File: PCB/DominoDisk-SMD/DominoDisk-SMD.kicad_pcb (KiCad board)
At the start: 2 copper layers, 45.7 x 38.9 mm, 33 parts, among them J1 Daisy port out, J2 ICSP_ISP6, J3 UART, J4 Daisy port in, K1 HYC77-TF09-200, U1 PC817C-S, U2 ATmega328P-AU, U3 SE5218, U4 TXB0104PWR, Y1 Resonator

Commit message: More OCD
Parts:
- J4: renamed from J3; moved to B.Cu
- moved R5 14.2 mm to (137.1, 51.9), turned to -90 degrees
- moved C7 3.84 mm to (117.9, 60.5), turned to 0 degrees
- moved J4 2.74 mm to (104.0, 67.4)
- moved R7 2.15 mm to (117.7, 52.3)
- moved C5 1.97 mm to (119.2, 52.3), turned to 90 degrees
- moved C6 1.92 mm to (122.5, 60.5)
- moved G*** 1.54 mm to (136.6, 60.0), turned to 90 degrees
- moved U4 1.53 mm to (120.2, 56.9)
- moved C4 1.52 mm to (125.0, 52.3)
- moved Y1 1.48 mm to (104.5, 62.5)
- moved U2 1.39 mm to (122.1, 52.3)
- moved C8 0.93 mm to (108.0, 62.7)
- moved R2 0.89 mm to (128.5, 53.2), turned to 0 degrees
- moved U3 0.78 mm to (107.0, 56.0)
- moved U1 0.25 mm to (132.3, 50.1)
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- renumbered C5 to C1, C6 to C2, C7 to C3, C8 to C4, C4 to C5, C9 to C6, C10 to C7, C2 to C8, D3 to D1, D1 to D2, D2 to D3, J4 to J3, R6 to R1, R4 to R2, R1 to R3, R3 to R4, R2 to R6, REF** to REF**1, REF** to REF**2, REF** to REF**3, REF** to REF**4, U3 to U2, U2 to U3
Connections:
- K1 pad SHIELD: (no net) -> GND
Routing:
- net HDSEL_in: track 8.24 -> 25.9 mm
- net 5V_burgerDisk: track 68.6 -> 56.3 mm, vias 5 -> 4
- net GND: track 124.4 -> 135.1 mm, vias 13 -> 11
- net WRPROT_out: track 40.6 -> 30.7 mm, vias 1 -> 2
- net DRV1_in: track 40.6 -> 45.6 mm
- net OE: track 4.05 -> 7.53 mm
- net TX: track 13.0 -> 16.3 mm
- net RESET: track 34.9 -> 37.8 mm
- net DRV2_out: track 35.3 -> 38.1 mm
- net WRPROT_in: track 44.1 -> 46.8 mm
- net Net-(U3-XTAL2/PB7): track 3.35 -> 1.20 mm
- net DRV2_burgerDisk: track 35.6 -> 37.6 mm
- net PH1: track 28.7 -> 27.3 mm
- net 3V3: track 21.2 -> 19.8 mm, vias 1 -> 2
- net PH0: track 25.8 -> 24.5 mm
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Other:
- board text added: "© Colin Leroy-Mira https://colino.net"

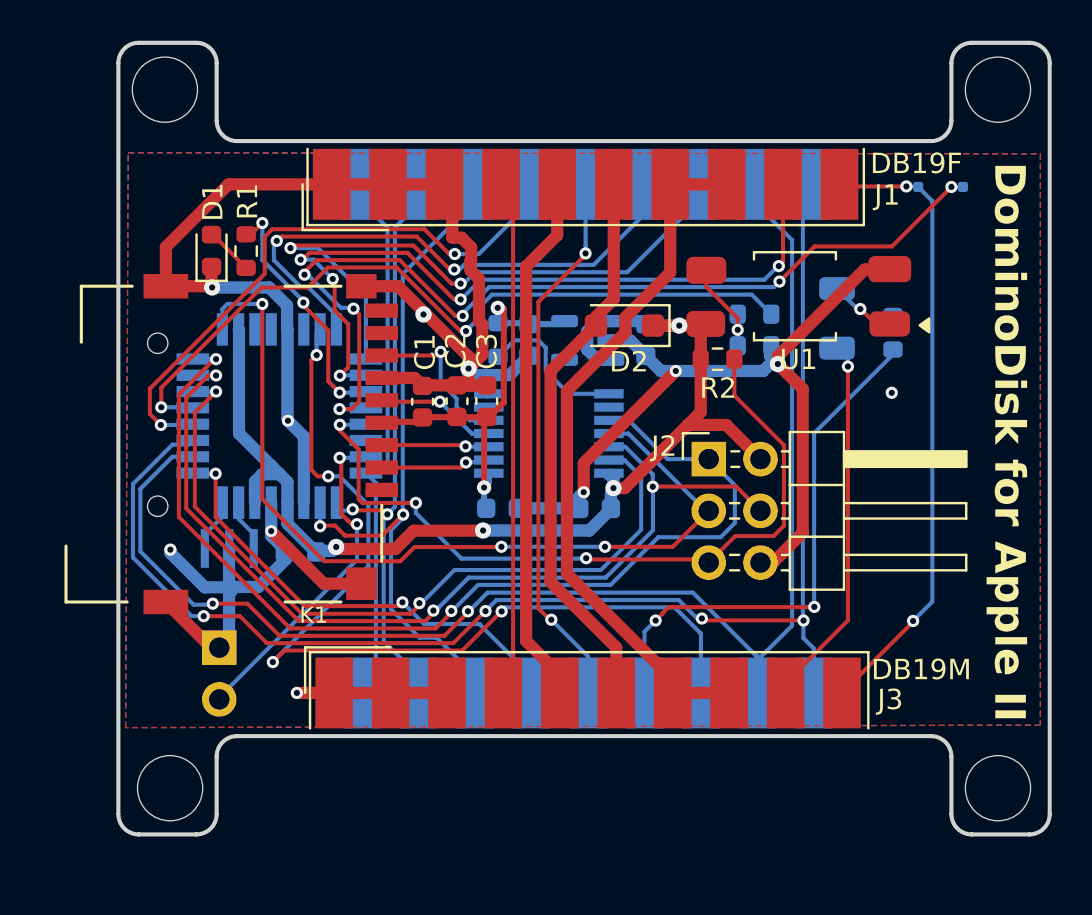
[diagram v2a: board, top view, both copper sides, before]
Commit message: Enable teardrops
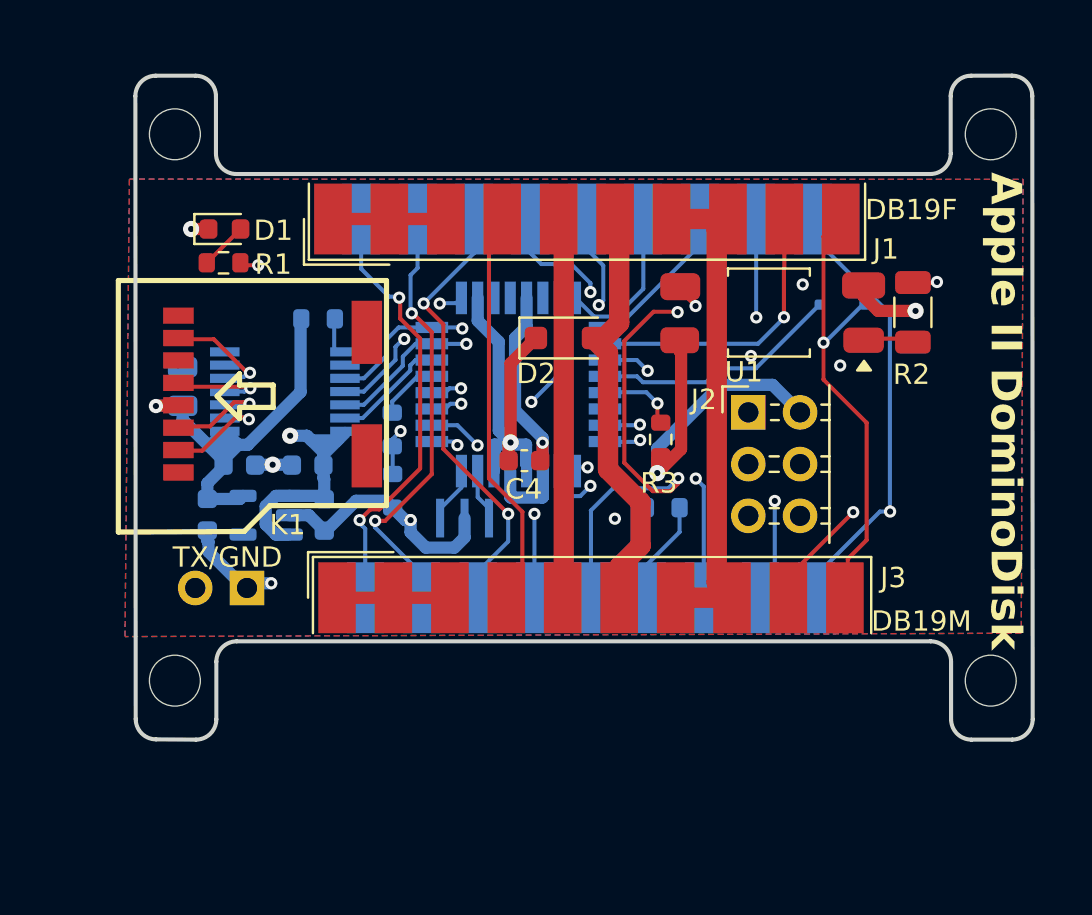
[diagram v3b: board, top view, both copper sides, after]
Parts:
- removed the C1 at (114.0, 55.3)
- removed the C2 at (115.7, 55.3)
- C1: renamed from C3; value 100n -> 22uF; footprint Capacitor_SMD:C_0603_1608Metric -> Capacitor_SMD:C_0805_2012Metric; moved to B.Cu
- C4: renamed from C8; moved to F.Cu
- J4: footprint Connector_PinHeader_2.54mm:PinHeader_1x02_P2.54mm_Horizontal -> Connector_PinHeader_2.54mm:PinHeader_1x02_P2.54mm_Vertical
- K1: value HYC77-TF09-200 -> TF-104; footprint HYC04-TF09-200:MICROSD-HYC77-TF09-200 -> TF-104:TF-SMD_TF-104
- R2: renamed from R3; moved to F.Cu
- REF**1, REF**2, REF**3, REF**4: value MountingHole_3.2mm_M3 -> MountingHole_2.5mm; footprint MountingHole:MountingHole_3.2mm_M3 -> MountingHole:MountingHole_2.5mm
- moved R6 19.1 mm to (112.5, 59.7), turned to 90 degrees
- moved R5 18.7 mm to (112.5, 56.7), turned to -90 degrees
- moved C5 18.0 mm to (109.2, 60.9)
- moved C6 18.0 mm to (103.5, 60.8)
- moved U4 18.0 mm to (106.3, 60.9)
- moved C1 14.9 mm to (102.2, 54.5)
- moved C2 14.3 mm to (108.4, 58.4)
- moved R7 14.2 mm to (125.8, 60.5), turned to 0 degrees
- moved U3 13.1 mm to (107.3, 54.8)
- moved C3 13.1 mm to (105.0, 58.4)
- moved C4 11.9 mm to (119.0, 58.2), turned to 0 degrees
- moved U2 11.8 mm to (118.7, 54.5)
- moved Y1 11.6 mm to (116.1, 61.0)
- moved R4 8.89 mm to (108.9, 51.2), turned to 0 degrees
- moved D3 7.53 mm to (134.6, 50.5), turned to 0 degrees
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- renumbered C6 to C2, C7 to C3, C4 to C5, C5 to C6, R2 to R3, R7 to R4, R4 to R5, R5 to R7, U3 to U2, U4 to U3, U2 to U4
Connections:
- K1 pad 9: (no net) -> GND
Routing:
- net GND: track 135.4 -> 48.7 mm, vias 11 -> 10
- net DRV2_burgerDisk: track 37.6 -> 3.00 mm, vias 2 -> 0
- net WRPROT_in: track 46.6 -> 12.2 mm, vias 6 -> 0
- net CS: track 37.6 -> 5.59 mm, vias 2 -> 0
- net MISO: track 50.8 -> 23.0 mm, vias 2 -> 1
- net RESET: track 37.8 -> 10.9 mm, vias 3 -> 1
- net RDDATA: track 66.3 -> 39.7 mm, vias 2 -> 3
- net DRV1_in: track 45.6 -> 21.8 mm, vias 4 -> 2
- net DRV2_out: track 37.7 -> 14.2 mm, vias 5 -> 1
- net DRV1_out: track 30.3 -> 6.93 mm, vias 2 -> 0
- net MOSI: track 46.9 -> 26.1 mm, vias 3 -> 1
- net HDSEL_in: track 25.9 -> 5.07 mm, vias 2 -> 0
- net WRDATA: track 68.2 -> 49.5 mm, vias 4 -> 2
- net Net-(R5-Pad2): track 5.36 -> 23.7 mm, vias 1 -> 2
- net HDSEL_out: track 25.0 -> 6.67 mm, vias 2 -> 0
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- added copper zone on In1.Cu, net GND
- added copper zone on In2.Cu, net GND
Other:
- board size 45.7 x 38.9 mm -> 44 x 32.6 mm
- copper layers 2 -> 4
- board text added: "Apple II DominoDisk"
- board text added: "TX/GND"
- board text added: "© Colin Leroy-Mira colino.net"
- board text removed: "DominoDisk for Apple II"
- board text removed: "© Colin Leroy-Mira https://colino.net"

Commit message: Better ground planes
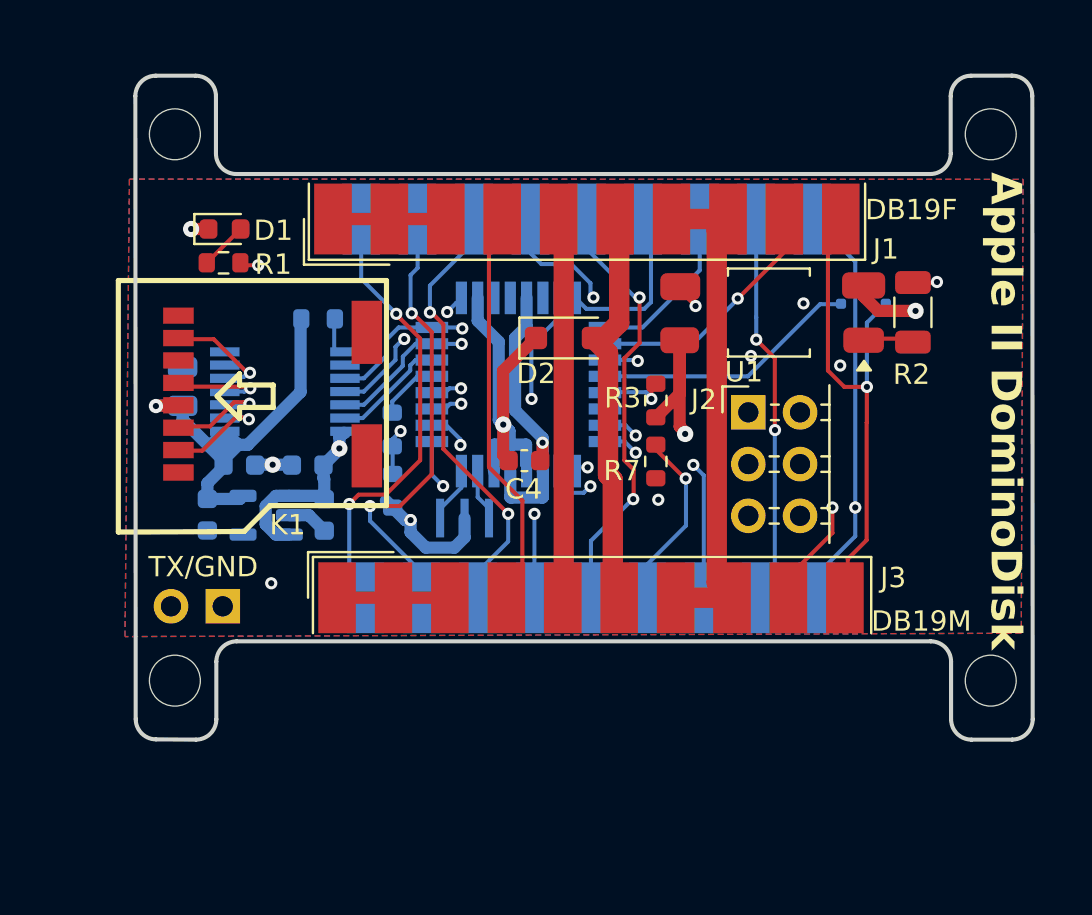
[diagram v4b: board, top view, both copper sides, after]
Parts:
- R7: moved to F.Cu
- moved R7 2.30 mm to (125.5, 58.2), turned to 90 degrees
- moved R3 1.93 mm to (125.5, 55.2)
- moved J4 1.49 mm to (104.2, 65.3)
- moved D3 1.05 mm to (135.7, 50.5)
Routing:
- net WREQ: track 29.3 -> 19.7 mm, vias 3 -> 2
- net GND: track 48.7 -> 40.4 mm
- net 5V_burgerDisk: track 70.5 -> 65.5 mm
- net HDSEL_in: track 5.07 -> 8.94 mm, vias 0 -> 1
- net TX: track 27.1 -> 29.4 mm
- net PH3_out: track 18.3 -> 15.9 mm
- net WRPROT_out: track 23.0 -> 25.2 mm
- net Net-(R5-Pad2): track 23.7 -> 21.6 mm
- net DRV2_out: track 14.2 -> 12.3 mm
- net WRDATA: track 49.5 -> 47.7 mm
- net HDSEL_out: track 6.67 -> 8.30 mm
- net RESET: track 10.9 -> 12.4 mm
- net PH3_in: track 10.7 -> 12.0 mm
- net LED: track 24.3 -> 23.0 mm
- net PH0: track 38.3 -> 39.2 mm
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
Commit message: micro changes
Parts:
- K1: value TF-104 -> TF-104 MicroSD card holder
- U3: value TXB0104PWR -> TXB0104PWR level shifter
- U4: value SE5218 -> SE5218 voltage regulator
- Y1: value Resonator -> CSTNE16M0V530000R0 Resonator

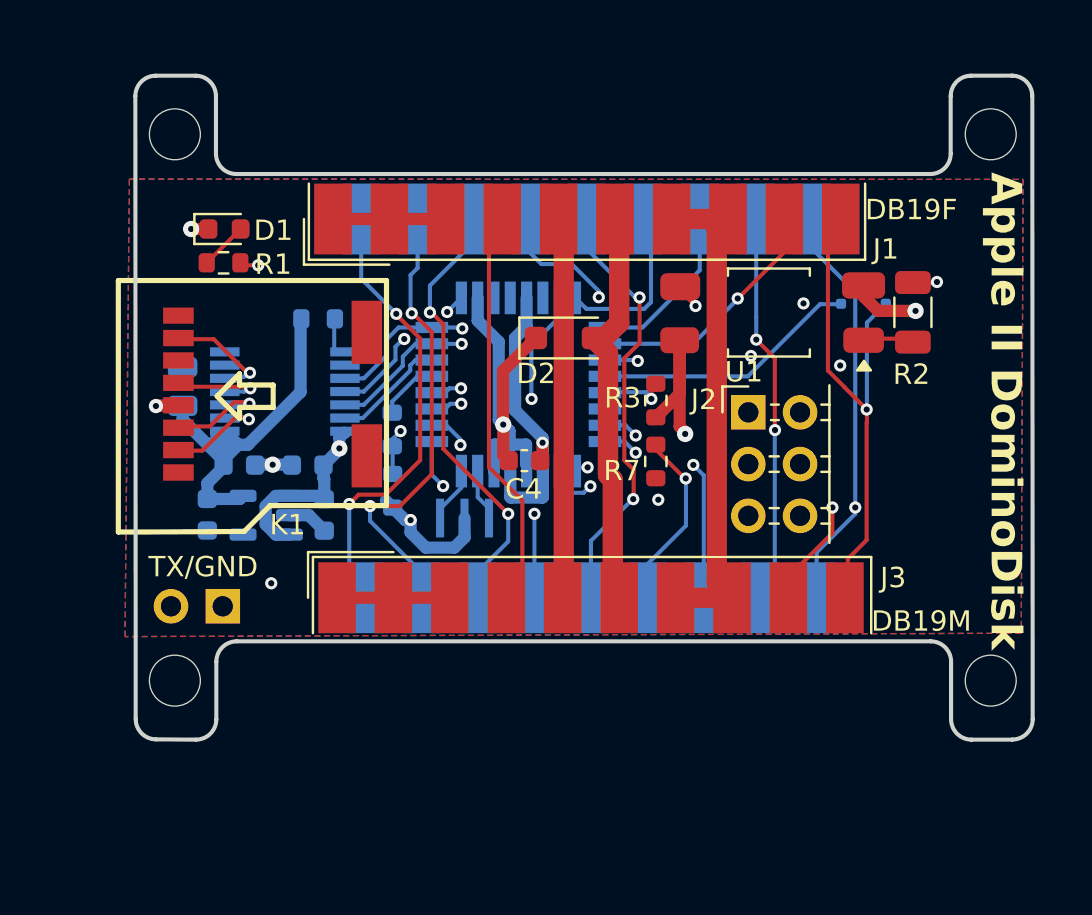
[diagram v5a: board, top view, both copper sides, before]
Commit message: Move logo out of PCB
until I'm sure Rebecca's estate is OK with it
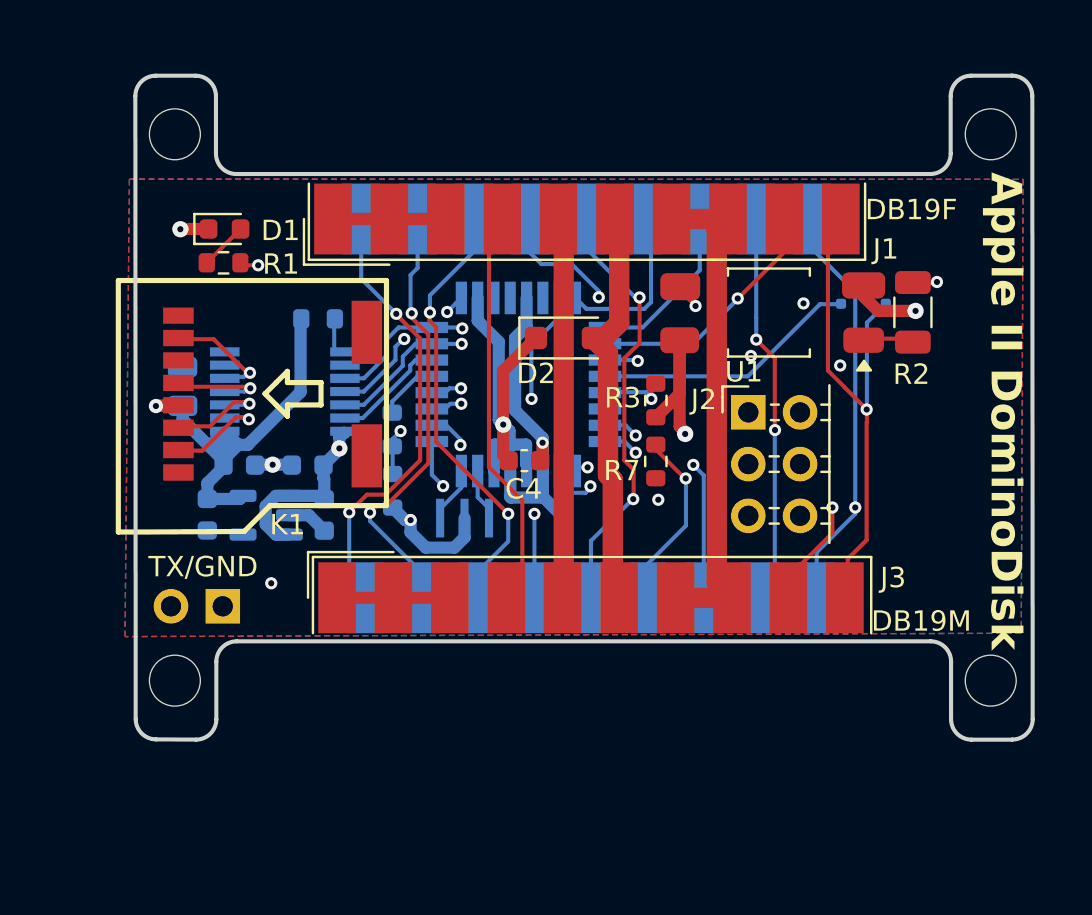
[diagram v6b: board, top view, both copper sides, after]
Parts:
- U4: value SE5218 voltage regulator -> SE5218ALG voltage regulator
- moved G*** 0.30 mm to (136.1, 56.0)
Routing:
- net WRDATA: track 47.7 -> 43.1 mm
- net PH2: track 29.0 -> 25.3 mm
- net EN3.5: track 19.9 -> 17.8 mm
- net PH1: track 34.5 -> 32.6 mm
- net RESET: track 12.4 -> 10.7 mm
- net DRV2_out: track 12.3 -> 10.7 mm
- net WRPROT_out: track 25.7 -> 24.6 mm
- net RDDATA: track 39.4 -> 38.4 mm
- net PH0: track 39.2 -> 38.2 mm
- net CS_L: track 5.42 -> 4.49 mm
- net 5V_apple2: track 20.1 -> 19.3 mm
- net GND: track 40.4 -> 41.1 mm
- net PH3_out: track 16.3 -> 15.6 mm
- net SCK: track 26.4 -> 25.7 mm
- net SCLK_L: track 4.96 -> 4.35 mm
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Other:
- board text added: "© Colin Leroy-Mira https://colino.net"
- board text removed: "© Colin Leroy-Mira colino.net"

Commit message: Cleanup for better ground
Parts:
- R7: moved to B.Cu
- moved C4 1.77 mm to (119.1, 56.4)
- moved D2 1.23 mm to (121.5, 53.3)
- moved U1 0.68 mm to (130.8, 51.5)
- moved R2 0.60 mm to (137.9, 51.5)
- moved C1 0.06 mm to (102.3, 54.5)
- turned R3 to 180 degrees
- turned R7 to -90 degrees
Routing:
- net 5V_burgerDisk: track 65.4 -> 54.9 mm
- net PH2: track 25.3 -> 32.3 mm
- net PH1: track 32.6 -> 37.5 mm
- net SCK: track 25.7 -> 30.1 mm
- net WRPROT_out: track 24.6 -> 28.3 mm
- net PH3_out: track 15.6 -> 19.2 mm
- net HDSEL_in: track 8.70 -> 6.04 mm, vias 1 -> 0
- net TX: track 29.4 -> 27.3 mm
- net DRV1_in: track 21.9 -> 20.0 mm
- net WREQ: track 19.7 -> 21.3 mm
- net EN3.5: track 17.8 -> 19.4 mm
- net -12V: track 18.3 -> 19.6 mm
- net RESET: track 10.7 -> 11.6 mm
- net HDSEL_out: track 7.77 -> 8.66 mm
- net Net-(R5-Pad2): track 21.4 -> 22.2 mm
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
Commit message: Rework for more cleanliness
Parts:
- J4: moved to F.Cu
- moved U1 6.85 mm to (123.9, 51.3)
- moved D2 6.79 mm to (121.7, 60.1)
- moved R3 6.34 mm to (119.2, 56.0), turned to 0 degrees
- moved R2 5.91 mm to (132.1, 52.4), turned to 180 degrees
- moved C4 1.75 mm to (119.1, 58.2)
- moved D3 1.34 mm to (134.3, 50.5)
- moved C2 0.93 mm to (108.6, 57.5)
- moved C5 0.93 mm to (109.4, 60.0)
- moved C6 0.93 mm to (103.7, 59.9)
- moved R4 0.93 mm to (109.1, 50.3)
- moved U4 0.93 mm to (106.6, 60.0)
- moved C3 0.93 mm to (105.2, 57.5)
- moved U3 0.93 mm to (107.5, 53.9)
- moved C1 0.20 mm to (102.5, 54.5)
- moved R6 0.12 mm to (112.4, 59.7)
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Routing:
- net WRPROT_out: track 28.3 -> 17.5 mm
- net GND: track 40.5 -> 50.8 mm
- net Net-(R5-Pad2): track 22.2 -> 13.5 mm
- net DRV2_in: track 19.4 -> 12.6 mm
- net LED: track 23.0 -> 28.4 mm
- net SCK: track 30.1 -> 25.0 mm
- net 3V3: track 24.3 -> 19.3 mm
- net PH3_out: track 19.2 -> 14.3 mm
- net RESET: track 11.6 -> 15.5 mm
- net DRV2_out: track 10.7 -> 13.1 mm
- net WREQ: track 21.3 -> 19.0 mm
- net 5V_burgerDisk: track 54.9 -> 56.9 mm, vias 3 -> 2
- net EN3.5: track 19.4 -> 17.5 mm
- net WRPROT_in: track 13.1 -> 11.7 mm
- net PH2: track 32.3 -> 33.5 mm
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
